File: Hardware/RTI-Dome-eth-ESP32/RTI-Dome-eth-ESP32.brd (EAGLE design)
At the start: 111.1 x 76.3 mm, 101 parts, among them IC1 REG1117FA-5.0_500, IC2 24LC64T-I/SN, IC8 REG1117-3.3V, J2 XT60PW-M, T1 MMBT3904LT1, T2 MMBT3904LT1, T3 MMBT3904LT1, U1 W5500, U2 ESP32-DevKitC ESP32-WROOM-32U, X9 J1011F01PNL

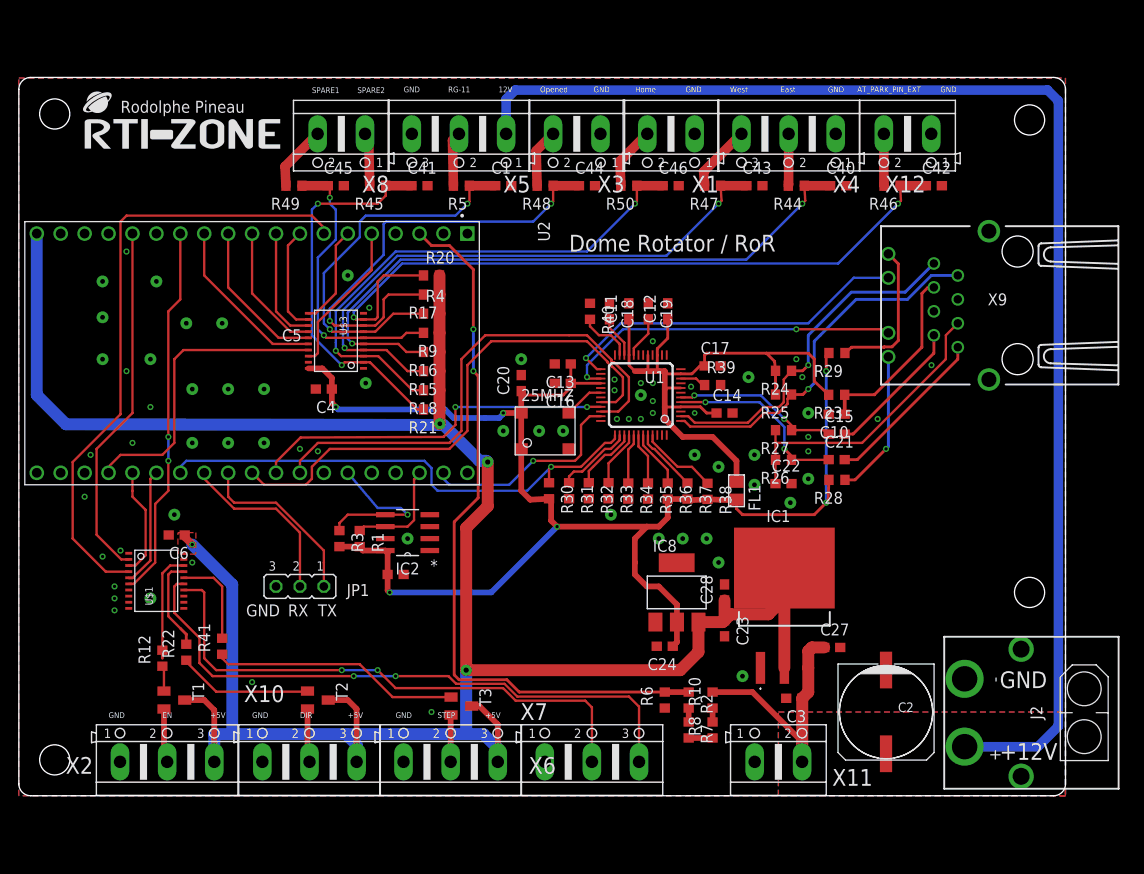
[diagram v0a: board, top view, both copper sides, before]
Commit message: Use switching regulator for the 5v. Can take from 8V to 40V in.
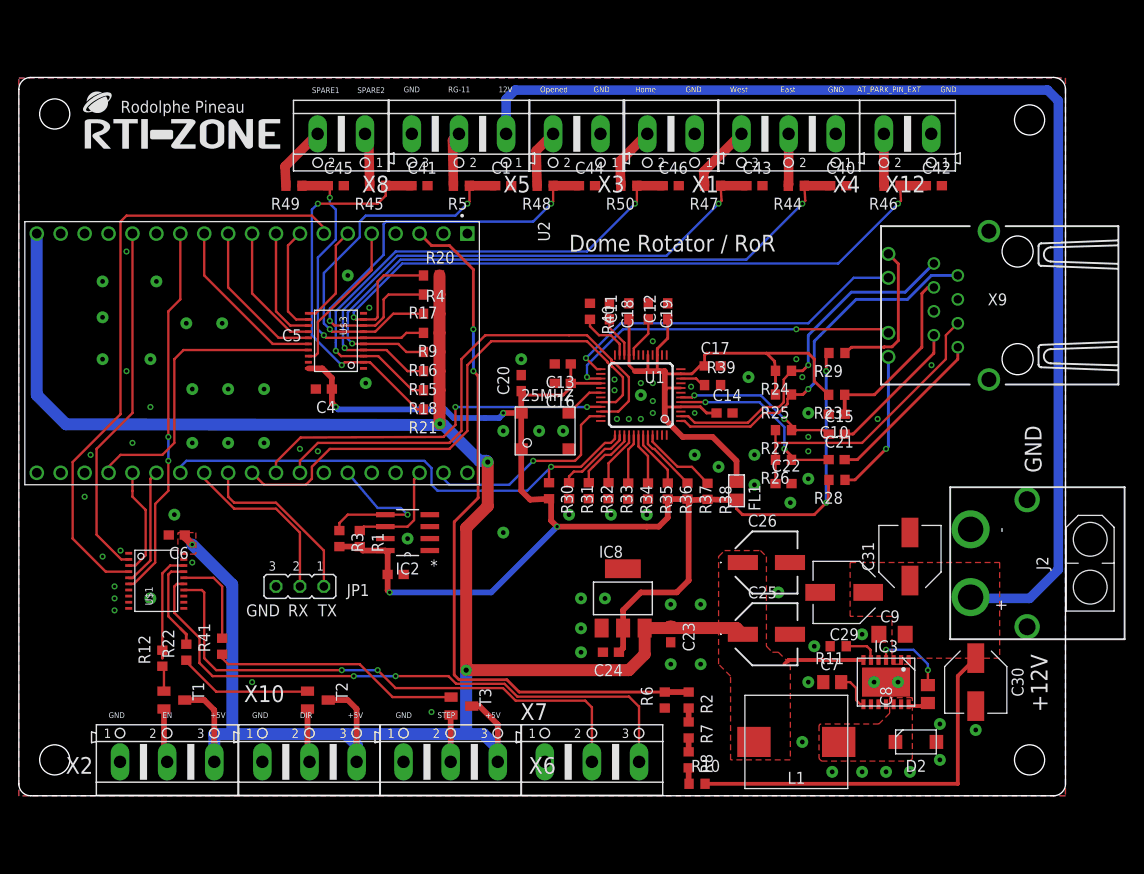
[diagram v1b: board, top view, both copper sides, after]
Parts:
- removed C2: 100uF, samacsys:UD-10X10_NICHICON
- removed C27, C28, C3: 10uF, rcl:C0603
- removed IC1: REG1117FA-5.0_500, REG1117FA-5.0_500:REG1117FA50500
- removed X11: (no value), rti:AK500/2
- added C25, C26: 180uF, samacsys:EEE0JA331XP
- added C29, C30, C31: 15uF 50V, samacsys:CAPAE660X550N
- added C7: 1nF, rcl:C0805
- added C8: 10nF, rcl:C0805
- added C9: 470nF, rcl:C1206
- added D2: VSSAF5L45-M3_6A, samacsys:SODFL5226X100N
- added IC3: LM2679SD-5.0_NOPB, samacsys:SON80P500X600X100-15N
- added L1: SRP1038CC-220M, samacsys:INDPM110100X400N
- added R11: 5.6K, rcl:R0603
- moved J2 15.9 mm to (101.1, 24.7)
- moved R10 9.04 mm to (72.0, 1.27), turned to 0 degrees
- moved C23 5.75 mm to (69.2, 17.1)
- moved C24 5.75 mm to (62.9, 15.2)
- moved IC8 5.75 mm to (64.1, 21.0)
- moved R8 4.07 mm to (71.1, 3.81), turned to 270 degrees
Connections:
- new net 5V_SW: C8.1, D2.1, IC3.12, IC3.13, IC3.14, L1.1
- new net CB: C8.2, IC3.4
- new net N$1: IC3.6, R11.1
- new net N$4: C7.2, IC3.8
- net +12V: now also C29.1, C30.1, C31.1, C9.2, IC3.2, IC3.3; no longer C2.+, C27.1, C3.1, IC1.3, X11.2
- net GND: now also C25.2, C26.2, C29.2, C30.2, C31.2, C7.1, C9.1, D2.2, IC3.15, IC3.9, R11.2; no longer C2.-, C27.2, C28.2, C3.2, IC1.1, X11.1
- net VCC: now also C25.1, C26.1, IC3.7, L1.2; no longer C28.1, IC1.2, IC1.4
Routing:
- net VCC: track 255.9 -> 243.1 mm
- net CB: track 0.00 -> 8.38 mm, vias 0 -> 2
- net 3.3V: track 153.1 -> 158.6 mm
- net N$4: track 0.00 -> 4.08 mm
- net N$1: track 0.00 -> 3.84 mm
- net 5V_SW: track 0.00 -> 2.26 mm
- net +12V: track 166.0 -> 164.6 mm
- net N$2: track 2.54 -> 1.47 mm
- added copper zone on layer 1, net 5V_SW
- removed copper zone on layer 16, net +12V

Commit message: Switch IO port to Wurth ones.
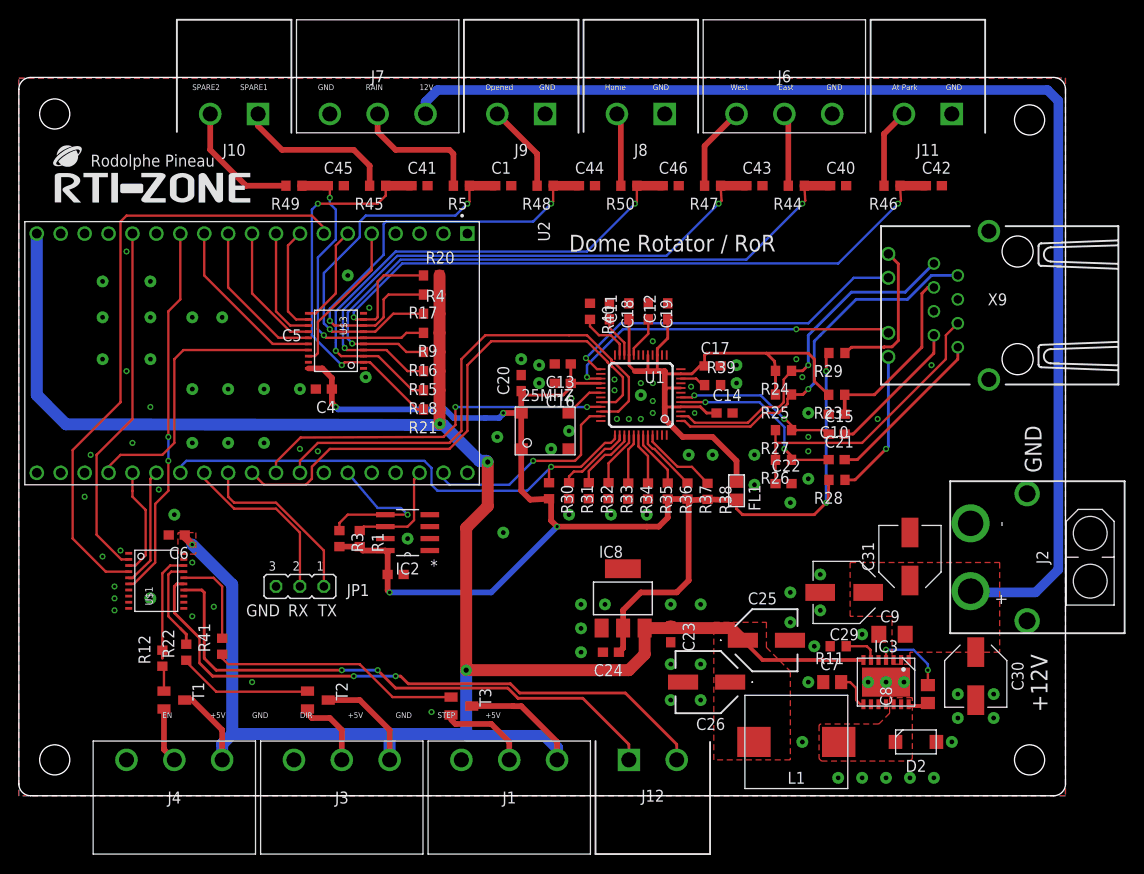
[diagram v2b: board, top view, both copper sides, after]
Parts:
- removed R10, R2, R6, R7, R8: 100K 0.1%, rcl:R0603
- removed X1, X12, X3, X8: (no value), rti:AK500/2
- removed X10, X2, X4, X5, X6, X7: (no value), rti:AK500/3
- added J1, J3, J4, J6, J7: 691313510003, samacsys:691313510003
- added J10, J11, J12, J8, J9: 691313510002, samacsys:SHDRRA2W100P0X508_1X2_1216X120
- moved C26 14.2 mm to (73.0, 12.1), turned to 180 degrees
- moved U$4 6.54 mm to (3.81, 63.0)
- moved C30 0.63 mm to (101.6, 12.7)
- moved C25 0.63 mm to (79.4, 16.5)
- moved J2 0.63 mm to (101.1, 25.3)
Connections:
- removed net N$2: R7.2, R8.1
- removed net N$3: R10.1, R8.2
- removed net N$5: R2.2, R7.1
- net +12V: now also J7.1; no longer R10.2, X5.1
- net AT_PARK_PIN-IN_EXT: now also J11.2; no longer X12.2
- net BUTTON_EAST_OPEN-IN_EXT: now also J6.2; no longer X4.2
- net BUTTON_WEST_CLOSE-IN_EXT: now also J6.3; no longer X4.3
- net DIR_5V_OUT: now also J3.2; no longer X10.2
- net EN_5V_OUT: now also J4.2; no longer X2.2
- net GND: now also J1.1, J11.1, J3.1, J4.1, J6.1, J7.3, J8.1, J9.1; no longer R6.1, X1.1, X10.1, X12.1, X2.1, X3.1, X4.1, X5.3, X6.1, X7.1
- net HOME_SHUTTER_CLOSED-IN_EXT: now also J8.2; no longer X1.2
- net RG-11-IN_EXT: now also J7.2; no longer X5.2
- net SHUTTER_OPENED-IN_EXT: now also J9.2; no longer X3.2
- net SPARE1-IN_EXT: now also J10.1; no longer X8.1
- net SPARE2-IN_EXT: now also J10.2; no longer X8.2
- net SPARE_OUT1_5V: now also J12.2; no longer X7.3
- net SPARE_OUT2_5V: now also J12.1; no longer X7.2
- net STEP_5V_OUT: now also J1.2; no longer X6.2
- net VCC: now also J1.3, J3.3, J4.3; no longer X10.3, X2.3, X6.3
- net VPIN: no longer R2.1, R6.2
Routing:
- net VPIN: track 77.3 -> 0.00 mm, vias 2 -> 0
- net +12V: track 164.6 -> 129.6 mm
- net VCC: track 243.1 -> 258.6 mm
- net SPARE1-IN_EXT: track 5.67 -> 17.0 mm
- net RG-11-IN_EXT: track 5.80 -> 14.3 mm
- net SPARE2-IN_EXT: track 6.95 -> 13.4 mm
- net STEP_5V_OUT: track 4.99 -> 9.56 mm
- net SHUTTER_OPENED-IN_EXT: track 6.26 -> 9.37 mm
- net AT_PARK_PIN-IN_EXT: track 5.51 -> 8.50 mm
- net DIR_5V_OUT: track 5.70 -> 8.02 mm
- net BUTTON_EAST_OPEN-IN_EXT: track 5.51 -> 7.79 mm
- net BUTTON_WEST_CLOSE-IN_EXT: track 7.18 -> 9.02 mm
- net N$3: track 1.72 -> 0.00 mm
- net N$5: track 1.48 -> 0.00 mm
- net N$2: track 1.47 -> 0.00 mm
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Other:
- board text added: "At Park"
- board text added: "RAIN"
- board text added: "Spare Out 1"
- board text added: "Spare Out 2"
- board text removed: "AT_PARK_PIN_EXT"
- board text removed: "RG-11"

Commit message: Now using Wurth connector for rotator and shutter.
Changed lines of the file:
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@@
 <attribute name="VALUE" x="38.1" y="78.295" size="1.27" layer="27" rot="R180" align="center"/>
 </element>
-<element name="J8" library="samacsys" library_urn="urn:adsk.eagle:library:37256869" package="SHDRRA2W100P0X508_1X2_1216X120" package3d_urn="urn:adsk.eagle:package:45454773/5" value="691313510002" x="66.04" y="72.39" smashed="yes" rot="R180">
+<element name="J8" library="samacsys" library_urn="urn:adsk.eagle:library:37256869" package="SHDRRA2W100P0X508_1X2_1216X120" package3d_urn="urn:adsk.eagle:package:45454773/6" value="691313510002" x="66.04" y="72.39" smashed="yes" rot="R180">
 <attribute name="ARROW_PART_NUMBER" value="" x="66.04" y="72.39" size="1.778" layer="27" rot="R180" display="off"/>
 <attribute name="ARROW_PRICE-STOCK" value="" x="66.04" y="72.39" size="1.778" layer="27" rot="R180" display="off"/>
@@
 <attribute name="MOUSER_PART_NUMBER" value="710-691313510002" x="66.04" y="72.39" size="1.778" layer="27" rot="R180" display="off"/>
 <attribute name="MOUSER_PRICE-STOCK" value="https://www.mouser.co.uk/ProductDetail/Wurth-Elektronik/691313510002?qs=2kOmHSv6VfR6BrMDgUh3kQ%3D%3D" x="66.04" y="72.39" size="1.778" layer="27" rot="R180" display="off"/>
-<attribute name="NAME" x="66.04" y="68.58" size="1.27" layer="25" rot="R180" align="center"/>
-<attribute name="VALUE" x="66.04" y="66.675" size="1.27" layer="27" rot="R180" align="center"/>
+<attribute name="NAME" x="66.04" y="76.2" size="1.27" layer="25" rot="R180" align="center"/>
+<attribute name="VALUE" x="66.04" y="78.105" size="1.27" layer="27" rot="R180" align="center"/>
 </element>
-<element name="J9" library="samacsys" library_urn="urn:adsk.eagle:library:37256869" package="SHDRRA2W100P0X508_1X2_1216X120" package3d_urn="urn:adsk.eagle:package:45454773/5" value="691313510002" x="53.34" y="72.39" smashed="yes" rot="R180">
+<element name="J9" library="samacsys" library_urn="urn:adsk.eagle:library:37256869" package="SHDRRA2W100P0X508_1X2_1216X120" package3d_urn="urn:adsk.eagle:package:45454773/6" value="691313510002" x="53.34" y="72.39" smashed="yes" rot="R180">
 <attribute name="ARROW_PART_NUMBER" value="" x="53.34" y="72.39" size="1.778" layer="27" rot="R180" display="off"/>
 <attribute name="ARROW_PRICE-STOCK" value="" x="53.34" y="72.39" size="1.778" layer="27" rot="R180" display="off"/>
@@
 <attribute name="MOUSER_PART_NUMBER" value="710-691313510002" x="53.34" y="72.39" size="1.778" layer="27" rot="R180" display="off"/>
 <attribute name="MOUSER_PRICE-STOCK" value="https://www.mouser.co.uk/ProductDetail/Wurth-Elektronik/691313510002?qs=2kOmHSv6VfR6BrMDgUh3kQ%3D%3D" x="53.34" y="72.39" size="1.778" layer="27" rot="R180" display="off"/>
-<attribute name="NAME" x="53.34" y="68.58" size="1.27" layer="25" rot="R180" align="center"/>
-<attribute name="VALUE" x="53.34" y="66.675" size="1.27" layer="27" rot="R180" align="center"/>
+<attribute name="NAME" x="53.34" y="76.2" size="1.27" layer="25" rot="R180" align="center"/>
+<attribute name="VALUE" x="53.34" y="78.105" size="1.27" layer="27" rot="R180" align="center"/>
 </element>
-<element name="J10" library="samacsys" library_urn="urn:adsk.eagle:library:37256869" package="SHDRRA2W100P0X508_1X2_1216X120" package3d_urn="urn:adsk.eagle:package:45454773/5" value="691313510002" x="22.86" y="72.39" smashed="yes" rot="R180">
+<element name="J10" library="samacsys" library_urn="urn:adsk.eagle:library:37256869" package="SHDRRA2W100P0X508_1X2_1216X120" package3d_urn="urn:adsk.eagle:package:45454773/6" value="691313510002" x="22.86" y="72.39" smashed="yes" rot="R180">
 <attribute name="ARROW_PART_NUMBER" value="" x="22.86" y="72.39" size="1.778" layer="27" rot="R180" display="off"/>
 <attribute name="ARROW_PRICE-STOCK" value="" x="22.86" y="72.39" size="1.778" layer="27" rot="R180" display="off"/>
@@
 <attribute name="MOUSER_PART_NUMBER" value="710-691313510002" x="22.86" y="72.39" size="1.778" layer="27" rot="R180" display="off"/>
 <attribute name="MOUSER_PRICE-STOCK" value="https://www.mouser.co.uk/ProductDetail/Wurth-Elektronik/691313510002?qs=2kOmHSv6VfR6BrMDgUh3kQ%3D%3D" x="22.86" y="72.39" size="1.778" layer="27" rot="R180" display="off"/>
-<attribute name="NAME" x="22.86" y="68.58" size="1.27" layer="25" rot="R180" align="center"/>
-<attribute name="VALUE" x="22.86" y="66.675" size="1.27" layer="27" rot="R180" align="center"/>
+<attribute name="NAME" x="22.86" y="76.2" size="1.27" layer="25" rot="R180" align="center"/>
+<attribute name="VALUE" x="22.86" y="78.105" size="1.27" layer="27" rot="R180" align="center"/>
 </element>
-<element name="J11" library="samacsys" library_urn="urn:adsk.eagle:library:37256869" package="SHDRRA2W100P0X508_1X2_1216X120" package3d_urn="urn:adsk.eagle:package:45454773/5" value="691313510002" x="96.52" y="72.39" smashed="yes" rot="R180">
+<element name="J11" library="samacsys" library_urn="urn:adsk.eagle:library:37256869" package="SHDRRA2W100P0X508_1X2_1216X120" package3d_urn="urn:adsk.eagle:package:45454773/6" value="691313510002" x="96.52" y="72.39" smashed="yes" rot="R180">
 <attribute name="ARROW_PART_NUMBER" value="" x="96.52" y="72.39" size="1.778" layer="27" rot="R180" display="off"/>
 <attribute name="ARROW_PRICE-STOCK" value="" x="96.52" y="72.39" size="1.778" layer="27" rot="R180" display="off"/>
@@
 <attribute name="MOUSER_PART_NUMBER" value="710-691313510002" x="96.52" y="72.39" size="1.778" layer="27" rot="R180" display="off"/>
 <attribute name="MOUSER_PRICE-STOCK" value="https://www.mouser.co.uk/ProductDetail/Wurth-Elektronik/691313510002?qs=2kOmHSv6VfR6BrMDgUh3kQ%3D%3D" x="96.52" y="72.39" size="1.778" layer="27" rot="R180" display="off"/>
-<attribute name="NAME" x="96.52" y="68.58" size="1.27" layer="25" rot="R180" align="center"/>
-<attribute name="VALUE" x="96.52" y="66.675" size="1.27" layer="27" rot="R180" align="center"/>
+<attribute name="NAME" x="96.52" y="76.2" size="1.27" layer="25" rot="R180" align="center"/>
+<attribute name="VALUE" x="96.52" y="78.105" size="1.27" layer="27" rot="R180" align="center"/>
 </element>
-<element name="J12" library="samacsys" library_urn="urn:adsk.eagle:library:37256869" package="SHDRRA2W100P0X508_1X2_1216X120" package3d_urn="urn:adsk.eagle:package:45454773/5" value="691313510002" x="67.31" y="3.81" smashed="yes">
+<element name="J12" library="samacsys" library_urn="urn:adsk.eagle:library:37256869" package="SHDRRA2W100P0X508_1X2_1216X120" package3d_urn="urn:adsk.eagle:package:45454773/6" value="691313510002" x="67.31" y="3.81" smashed="yes">
 <attribute name="ARROW_PART_NUMBER" value="" x="67.31" y="3.81" size="1.778" layer="27" display="off"/>
 <attribute name="ARROW_PRICE-STOCK" value="" x="67.31" y="3.81" size="1.778" layer="27" display="off"/>
